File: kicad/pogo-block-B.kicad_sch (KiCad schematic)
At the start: 8 parts, among them J29 MAIN_L, J30 MAIN_R, U61 TL072, U62 TL072

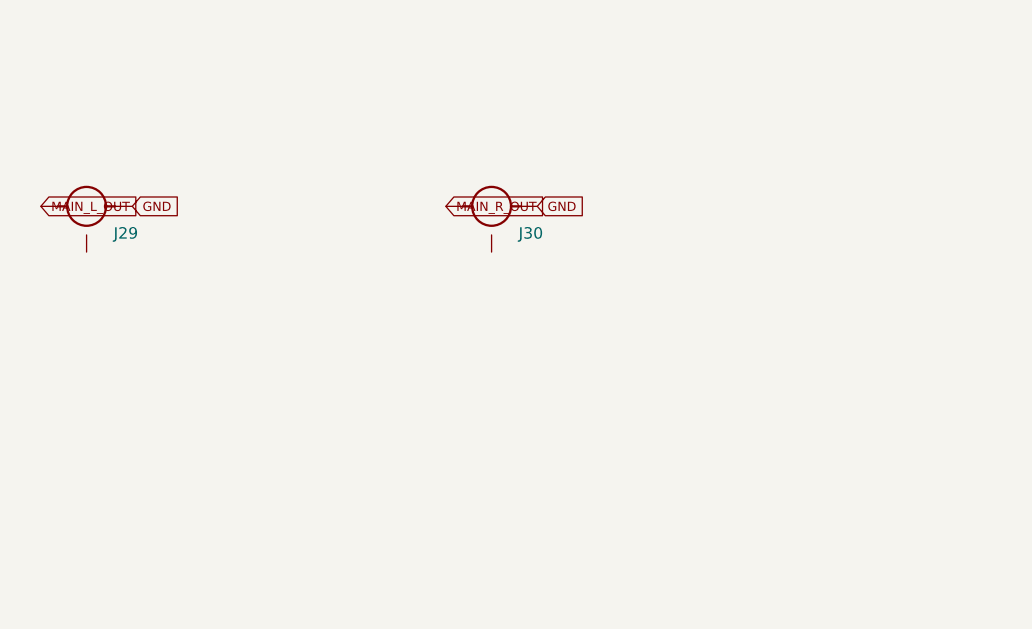
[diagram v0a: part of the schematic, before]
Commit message: components: add U61/U62 decoupling caps (C37-C40); wire into block-B
Resolve the flagged block-B drift: components.yaml had no decoupling for the
output-buffer op-amps while every other dual op-amp gets 2x 100nF. Add C37-C40
(audio board, next free C refs after block-8's C36) and wire them into the
block-B netlist (+12V/-12V to GND per IC). Regenerated BOM (281 rows) and
block-B schematic (12 parts). All gates green.
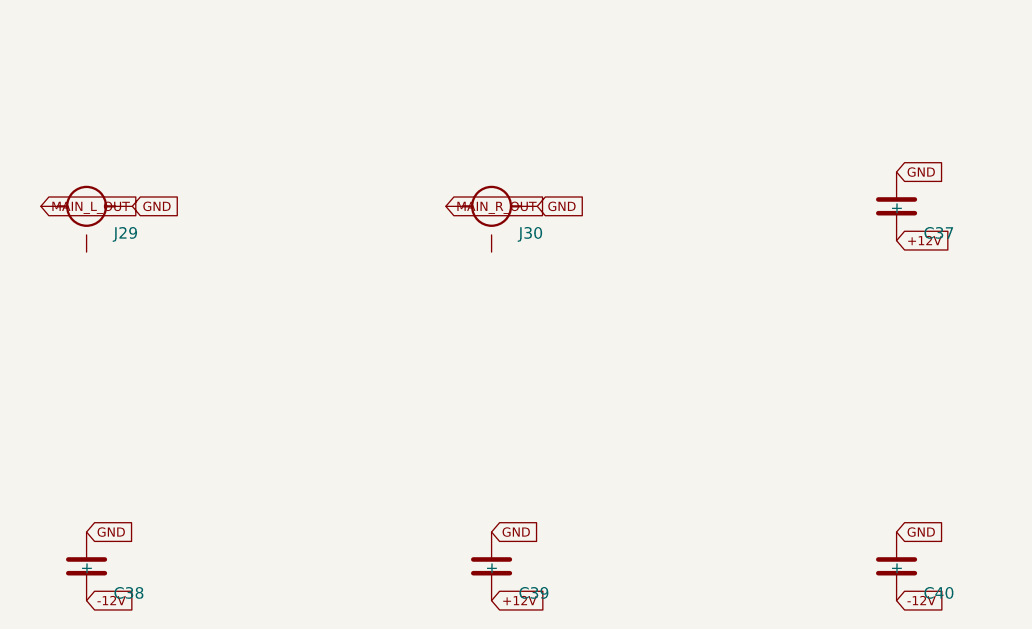
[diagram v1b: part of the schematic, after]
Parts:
- added C37, C38, C39, C40: 100nF, symbol Device:C
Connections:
- net +12V: now also C37.2, C39.2
- net -12V: now also C38.2, C40.2
- net GND: now also C37.1 (+), C38.1 (+), C39.1 (+), C40.1 (+)
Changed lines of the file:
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@@
     (effects (font (size 1.016 1.016)) (hide yes)))
+)
+(symbol
+  (lib_id "Device:C")
+  (at 130.000 120.000 0)
+  (unit 1)
+  (in_bom yes)
+  (on_board yes)
+  (property "Reference" "C37" (at 133.000 123.000 0)
+    (effects (font (size 1.27 1.27)) (justify left)))
+  (property "Value" "100nF" (at 133.000 119.500 0)
+    (effects (font (size 1.016 1.016)) (justify left) (hide yes)))
+)
+(symbol
+  (lib_id "Device:C")
+  (at 40.000 160.000 0)
+  (unit 1)
+  (in_bom yes)
+  (on_board yes)
+  (property "Reference" "C38" (at 43.000 163.000 0)
+    (effects (font (size 1.27 1.27)) (justify left)))
+  (property "Value" "100nF" (at 43.000 159.500 0)
+    (effects (font (size 1.016 1.016)) (justify left) (hide yes)))
+)
+(symbol
+  (lib_id "Device:C")
+  (at 85.000 160.000 0)
+  (unit 1)
+  (in_bom yes)
+  (on_board yes)
+  (property "Reference" "C39" (at 88.000 163.000 0)
+    (effects (font (size 1.27 1.27)) (justify left)))
+  (property "Value" "100nF" (at 88.000 159.500 0)
+    (effects (font (size 1.016 1.016)) (justify left) (hide yes)))
+)
+(symbol
+  (lib_id "Device:C")
+  (at 130.000 160.000 0)
+  (unit 1)
+  (in_bom yes)
+  (on_board yes)
+  (property "Reference" "C40" (at 133.000 163.000 0)
+    (effects (font (size 1.27 1.27)) (justify left)))
+  (property "Value" "100nF" (at 133.000 159.500 0)
+    (effects (font (size 1.016 1.016)) (justify left) (hide yes)))
 )
 (global_label "+12V"
@@
   (shape input)
   (at 85.000 47.620 0)
+  (effects (font (size 1.016 1.016)) (justify left))
+)
+(global_label "+12V"
+  (shape input)
+  (at 130.000 123.810 0)
+  (effects (font (size 1.016 1.016)) (justify left))
+)
+(global_label "+12V"
+  (shape input)
+  (at 85.000 163.810 0)
   (effects (font (size 1.016 1.016)) (justify left))
 )
@@
   (effects (font (size 1.016 1.016)) (justify left))
 )
+(global_label "-12V"
+  (shape input)
+  (at 40.000 163.810 0)
+  (effects (font (size 1.016 1.016)) (justify left))
+)
+(global_label "-12V"
+  (shape input)
+  (at 130.000 163.810 0)
+  (effects (font (size 1.016 1.016)) (justify left))
+)
 (global_label "GND"
   (shape input)
@@
   (effects (font (size 1.016 1.016)) (justify left))
 )
+(global_label "GND"
+  (shape input)
+  (at 130.000 116.190 0)
+  (effects (font (size 1.016 1.016)) (justify left))
+)
+(global_label "GND"
+  (shape input)
+  (at 40.000 156.190 0)
+  (effects (font (size 1.016 1.016)) (justify left))
+)
+(global_label "GND"
+  (shape input)
+  (at 85.000 156.190 0)
+  (effects (font (size 1.016 1.016)) (justify left))
+)
+(global_label "GND"
+  (shape input)
+  (at 130.000 156.190 0)
+  (effects (font (size 1.016 1.016)) (justify left))
+)

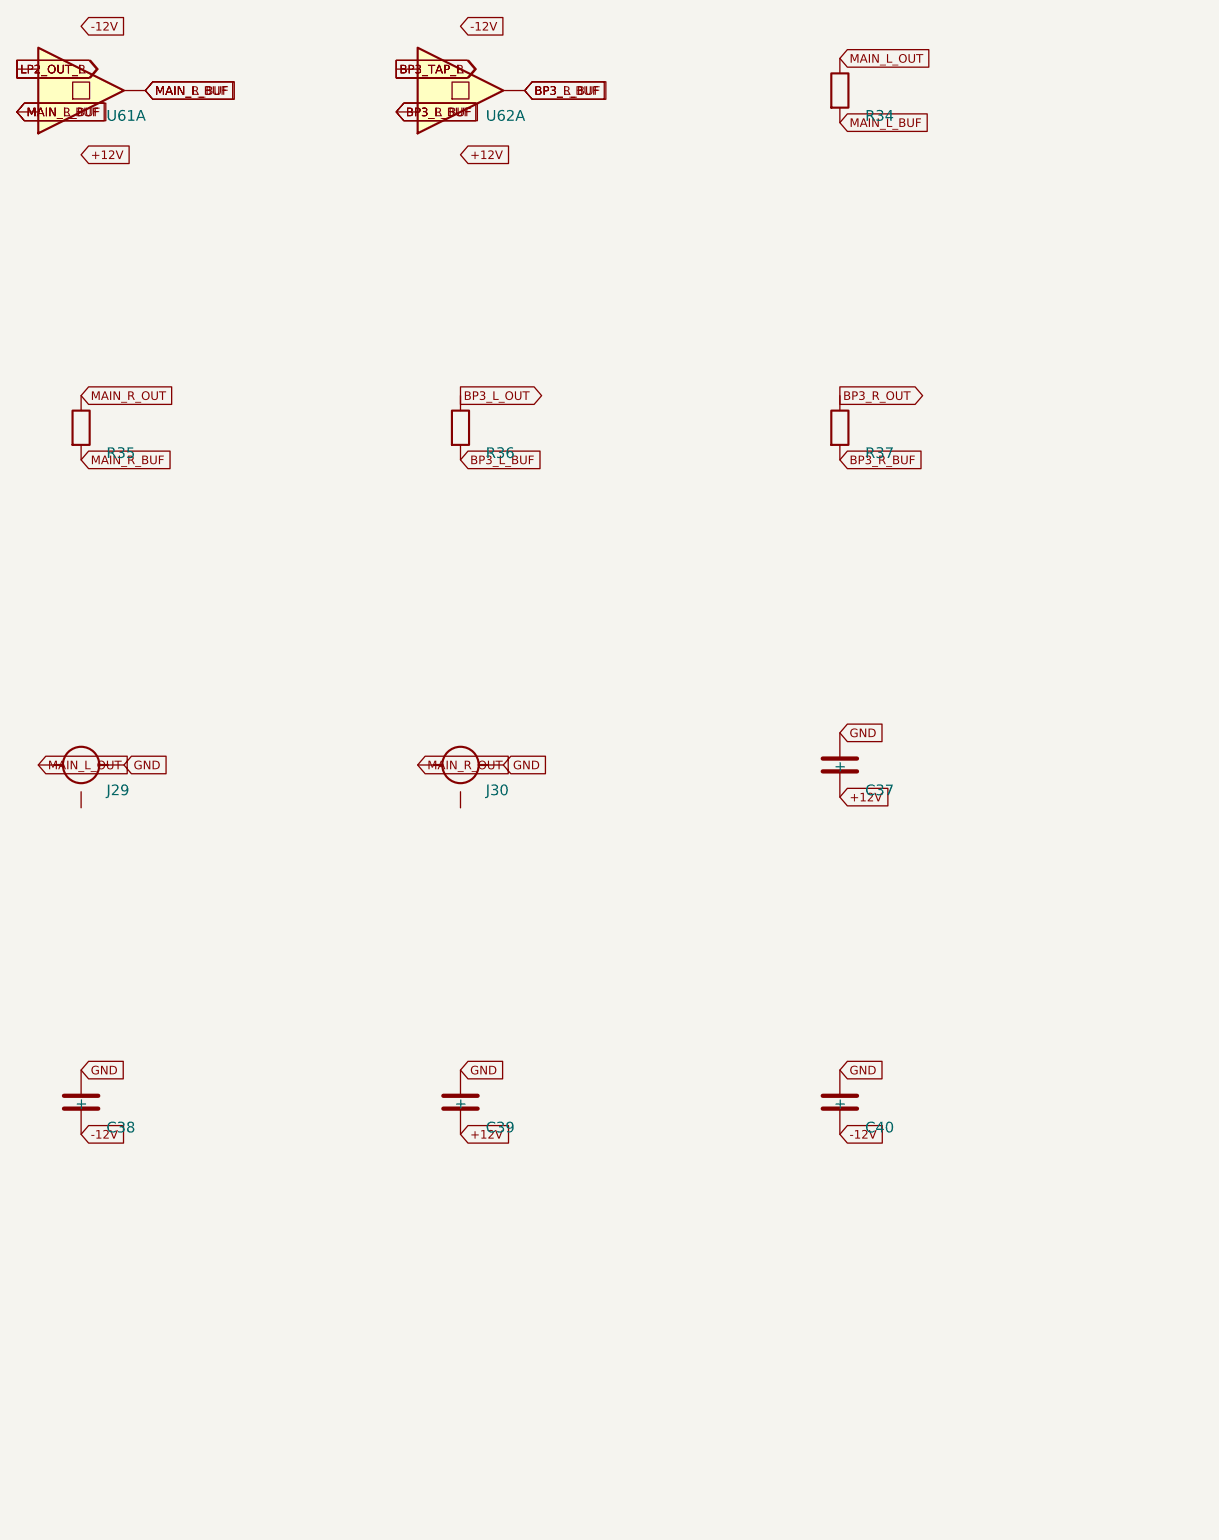
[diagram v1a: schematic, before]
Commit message: kicad: block-8 LP2 + fix multi-unit op-amp placement bug (7 of 10)
block-8 (LP2): OTA-C SVF mirroring LP1 minus tilt (single shared expo); Q VCA via
the shared-q sheet cell B (U9/U10); added LP2's own IRES_AMP (U65, was missing from
the BOM) + full SVF expansion (R_LIN, expo network, Q V->I, buffer pulldowns,
decoupling). 51 parts / 36 nets; LP2 boundary nets match shared-q byte-for-byte.
shared-q gains the LP2 cell-B Iabc bypass caps (C84/C85).

GENERATOR CORRECTNESS FIX (exposed by block-8's spare op-amp half): dual op-amps
were placed as a single instance while pins from BOTH halves were connected at the
lib_symbol's overlapping origin -> unit-A and unit-B pins landed on the same canvas
point, shorting the two halves. This was latent in EVERY dual-op-amp block (A,B,1,2,
4,5). Fix:
- place each gate unit (A/B/power) as its own instance at distinct offsets
  (MULTI_UNIT + opamp_unit_pins);
- make structural_check unit-aware (per-sub-symbol unit pins);
- add a short detector: 2+ distinct nets whose labels coincide at one point now fail.
All blocks regenerated and re-verified clean (the detector finds no shorts).

STATUS+plan: 7/10 blocks. All gates green.
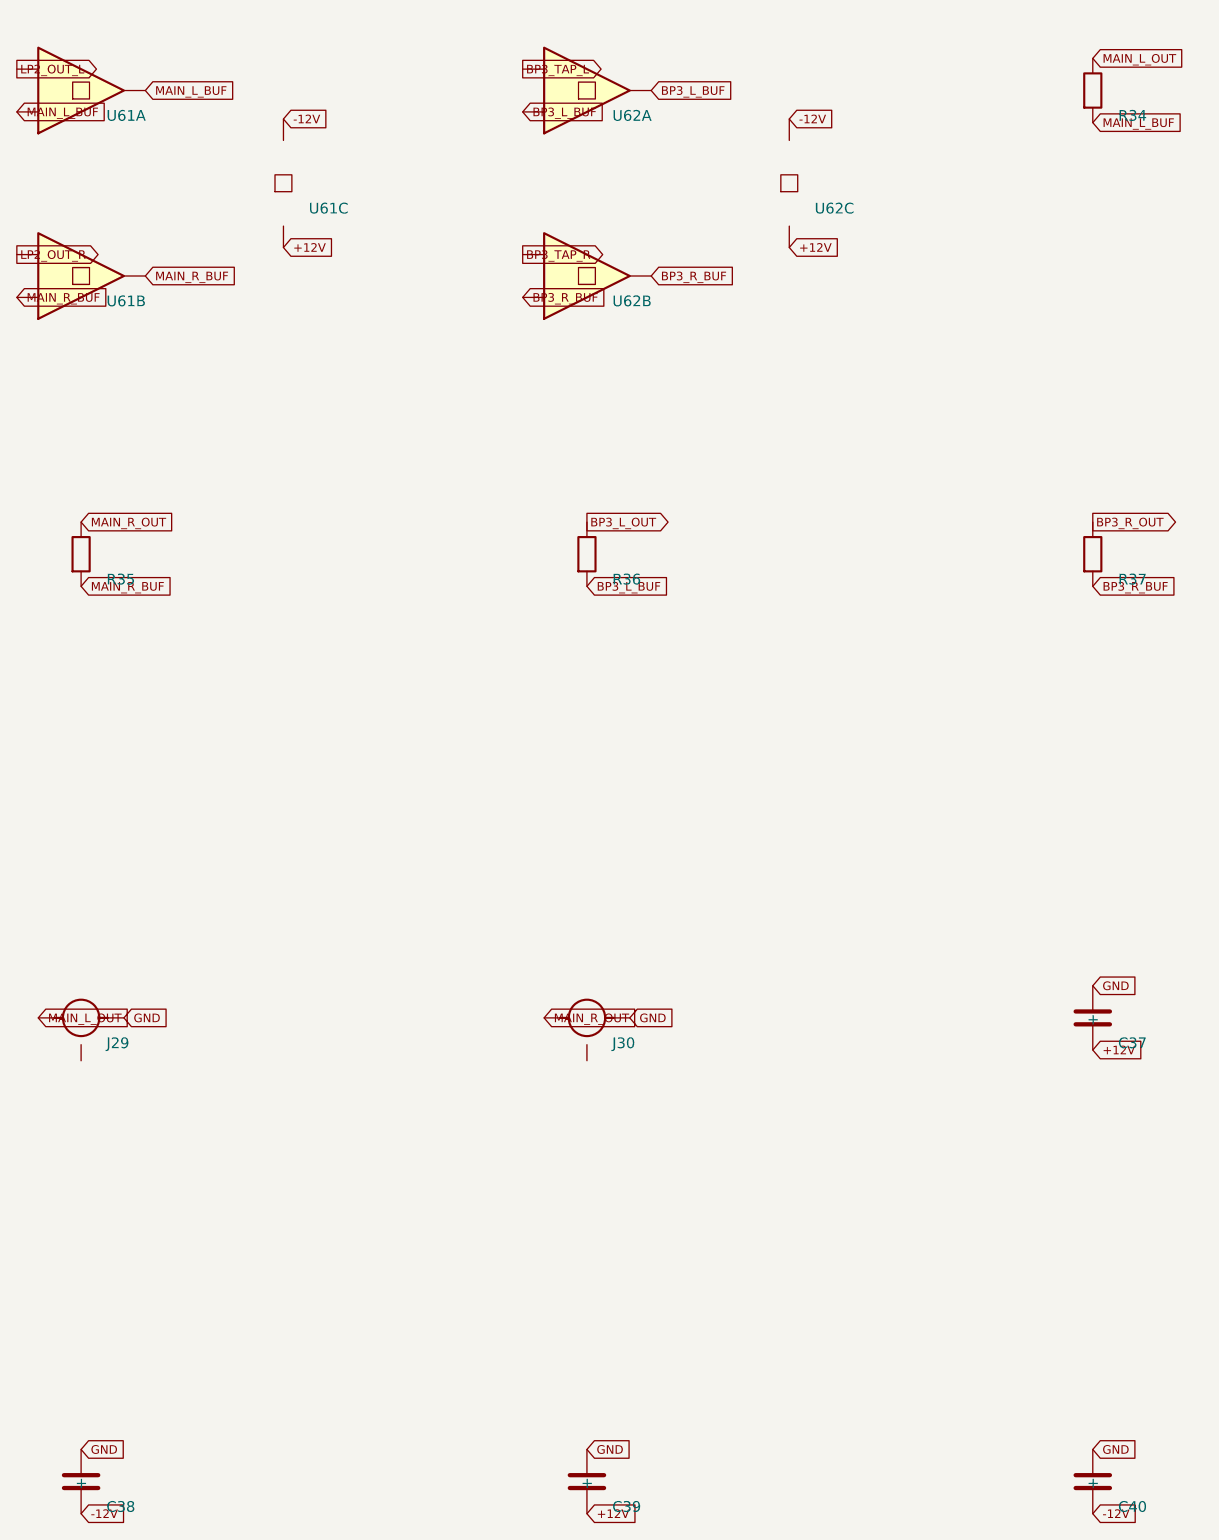
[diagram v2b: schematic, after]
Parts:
- added C37, C38, C39, C40: 100nF, symbol Device:C
- J29: renamed from C39; value 100nF -> MAIN_L; footprint (none) -> POGO_Connector_Audio:Jack_3.5mm_QingPu_WQP-PJ398SM_Vertical_CircularHoles; symbol Device:C -> Device:Audio_Jack_3.5mm_SwitchT
- J30: renamed from C40; value 100nF -> MAIN_R; footprint (none) -> POGO_Connector_Audio:Jack_3.5mm_QingPu_WQP-PJ398SM_Vertical_CircularHoles; symbol Device:C -> Device:Audio_Jack_3.5mm_SwitchT
- R34: renamed from J29; value MAIN_L -> 1k; footprint POGO_Connector_Audio:Jack_3.5mm_QingPu_WQP-PJ398SM_Vertical_CircularHoles -> (none); symbol Device:Audio_Jack_3.5mm_SwitchT -> Device:R
- R35: renamed from J30; value MAIN_R -> 1k; footprint POGO_Connector_Audio:Jack_3.5mm_QingPu_WQP-PJ398SM_Vertical_CircularHoles -> (none); symbol Device:Audio_Jack_3.5mm_SwitchT -> Device:R
- R36: renamed from C37; value 100nF -> 1k; symbol Device:C -> Device:R
- R37: renamed from C38; value 100nF -> 1k; symbol Device:C -> Device:R
- U61: renamed from R34; value 1k -> TL072; symbol Device:R -> Amplifier_Operational:OPA1612
- U61: renamed from U62; footprint POGO_Package_SO:SOIC-8_3.9x4.9mm_P1.27mm -> (none)
- U62: renamed from R36; value 1k -> TL072; symbol Device:R -> Amplifier_Operational:OPA1612
- U62: renamed from R35; value 1k -> TL072; footprint (none) -> POGO_Package_SO:SOIC-8_3.9x4.9mm_P1.27mm; symbol Device:R -> Amplifier_Operational:OPA1612
- U62: renamed from R37; value 1k -> TL072; symbol Device:R -> Amplifier_Operational:OPA1612
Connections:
- net +12V: now also U61.4 (V-), U62.4 (V-), C37.2, C39.2; no longer J29.2, R36.2
- net -12V: now also U61.8 (V+), U62.8 (V+), C38.2, C40.2; no longer J30.2, R37.2
- net BP3_L_BUF: now also R36.2, U62.1 (Out), U62.3 (In+); no longer U61.1 (Out), U61.3 (In+), U62.2, U62.2
- net BP3_L_OUT: now also R36.1; no longer U62.1
- net BP3_R_OUT: now also R37.1; no longer U62.1
- net BP3_TAP_L: now also U62.2 (In-); no longer U61.2 (In-)
- net GND: now also J29.2 (S), J30.2 (S), C37.1 (+), C38.1 (+), C39.1 (+), C40.1 (+); no longer J29.1 (+), J30.1 (+), R34.2 (S), R35.2 (S), R36.1 (+), R37.1 (+)
- net MAIN_L_BUF: now also R34.2; no longer U61.2, U62.2
- net MAIN_L_OUT: now also J29.1 (T); no longer U61.1
- net MAIN_R_OUT: now also J30.1 (T); no longer U62.1
- new net BP3_R_BUF: R37.2, U62.5 (In+), U62.7 (Out)
- new net BP3_TAP_R: U62.6 (In-)
- new net LP2_OUT_R: U61.6 (In-)
- new net MAIN_R_BUF: R35.2, U61.5 (In+), U61.7 (Out)
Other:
- moved on the sheet: U61B, U61C, U62C
